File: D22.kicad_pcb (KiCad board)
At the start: 6 copper layers, 15 x 11 mm, 48 parts, among them IC1 AVR64DD28-I_STX, IC2 NCP730BM, IC3 DRV8231ADSGR, J1 Conn_02x08_Counter_Clockwise, J2 Conn_01x01, J3 Conn_01x01, J4 Conn_01x01, Q1 BC847BDW1, Q2 BC857BDW1, Q3 PMZB200UNEYL, Q4 PMZB200UNEYL, Q5 PMZB200UNEYL, Q6 PMZB200UNEYL

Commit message: mod: code cleanup
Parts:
- removed C4: 22u/25V, Capacitor_SMD:C_0603_1608Metric
- removed C7: 10u/25V, Capacitor_SMD:C_0603_1608Metric
- removed J3, J4: Conn_01x01, RTB:DummyNet-Connector
- added D4: SM5819L2-TP, RTB:SM5819L2TP, B.Cu at (62.5, -45.4)
- added IC4: NCP730BM, Package_SON:WSON-6-1EP_2x2mm_P0.65mm_EP1x1.6mm, B.Cu at (65.9, -46.0)
- added R23: 100, Resistor_SMD:R_0603_1608Metric, B.Cu at (62.1, -46.7)
- added R24: 10k, Resistor_SMD:R_0402_1005Metric, B.Cu at (59.5, -47.9)
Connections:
- net SUSI.dat renamed CAP_ENA
- IC1 pad 22: (no net) -> unconnected-(IC1-PF6_(~{RESET})-Pad22)
- IC2 pad 2: Net-(IC2-Pad2) -> unconnected-(IC2-NC/ADJ-Pad2)
- IC2 pad 4: (no net) -> unconnected-(IC2-EN-Pad4)
- IC2 pad 5: (no net) -> unconnected-(IC2-NC/PG-Pad5)
- J1 pad 14: VHBR -> CAP+
- J1 pad 7: (no net) -> unconnected-(J1-Pin_7-Pad7)
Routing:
- net CAP+: track 0.00 -> 5.32 mm, vias 0 -> 1
- net Net-(IC4-OUT): track 0.00 -> 4.81 mm
- net VHBR: track 22.0 -> 18.3 mm, vias 5 -> 2
- net CAP_ENA: track 19.5 -> 22.5 mm, vias 1 -> 2
- net +3V3: track 27.0 -> 26.1 mm
- net GND: track 32.9 -> 33.8 mm, vias 13 -> 12
- net AUX3: track 15.4 -> 14.8 mm
- net M1: track 23.4 -> 22.7 mm
- net SUSI.clk: vias 2 -> 1
- added copper zone on B.Cu, net unconnected-(IC2-NC/ADJ-Pad2)
- removed copper zone on B.Cu, net Net-(IC2-Pad2)
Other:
- board text added: "D22.1"
- board text removed: "D22.0"

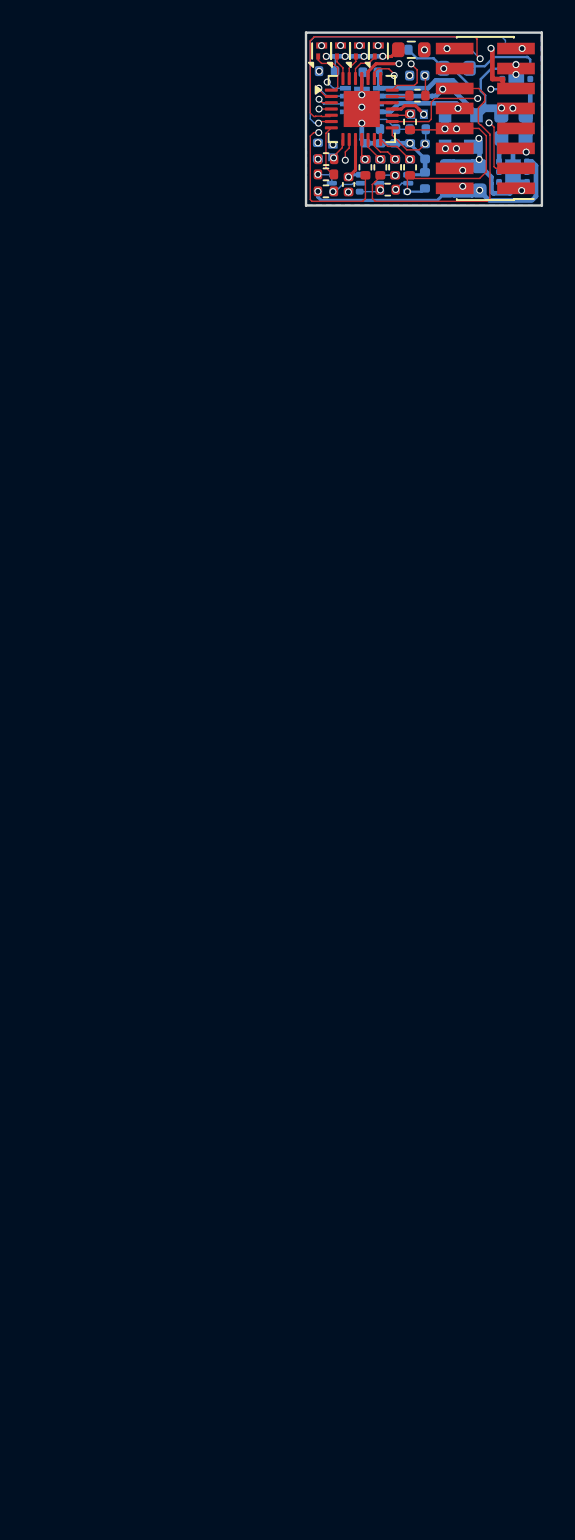
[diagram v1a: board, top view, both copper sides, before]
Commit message: add: 15V LDO for backup cap
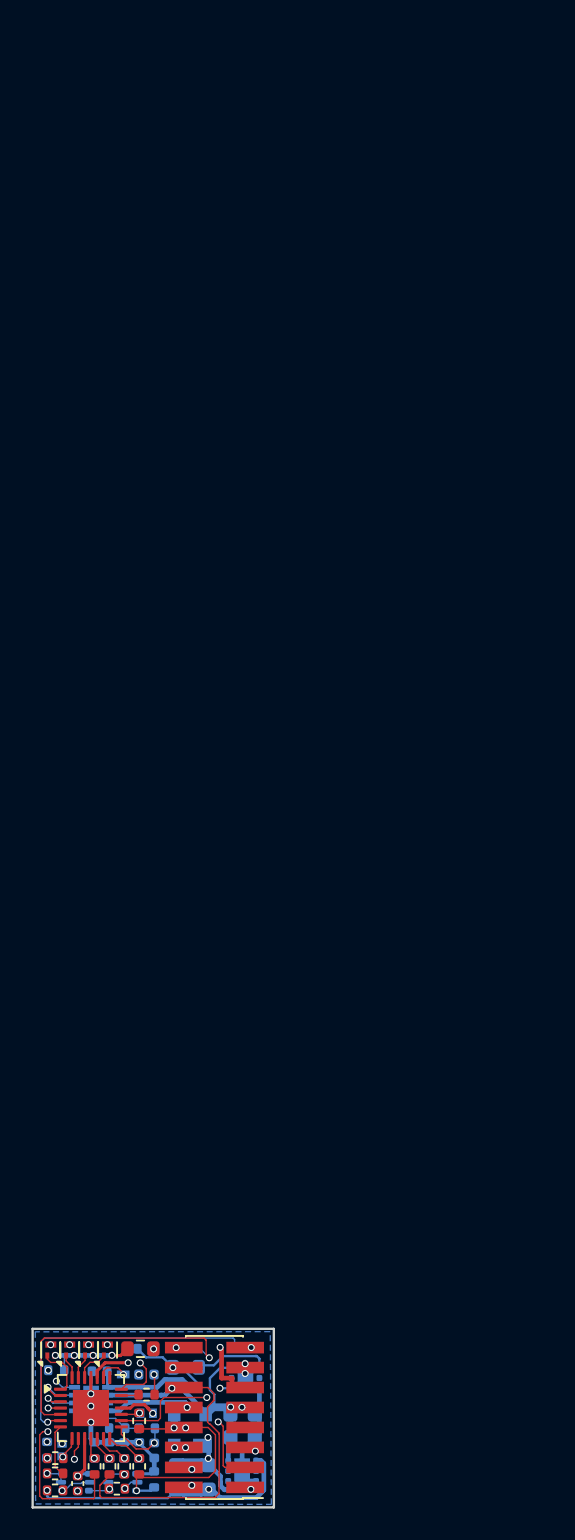
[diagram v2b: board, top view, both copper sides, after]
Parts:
- C1, C2: value 22u/25V -> 10u/25V
- C10, C8: value 100n -> 100n/50V
- C6: value 1u -> 1u/50V
- IC2: value NCP730BM -> NCP730BMT500TBG
- IC4: value NCP730BM -> NCP730BMT1500TBG
- J2: footprint RTB:DummyNet-Connector -> RTB:Solder 0.8 x 0.5
- moved C1 84.4 mm to (48.5, 40.4)
- moved C10 84.4 mm to (39.4, 36.2)
- moved C2 84.4 mm to (48.5, 39.0)
- moved C3 84.4 mm to (44.3, 43.0)
- moved C5 84.4 mm to (46.3, 43.0)
- moved C6 84.4 mm to (42.8, 41.3)
- moved C8 84.4 mm to (38.0, 43.4)
- moved D1 84.4 mm to (42.4, 38.9)
- moved D2 84.4 mm to (37.0, 41.2)
- moved D3 84.4 mm to (42.3, 36.4)
- moved D4 84.4 mm to (45.2, 37.3)
- moved D8 84.4 mm to (45.1, 40.3)
- moved IC1 84.4 mm to (38.8, 38.6)
- moved IC2 84.4 mm to (48.4, 42.6)
- moved IC3 84.4 mm to (38.8, 38.0)
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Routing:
- net CAP_ENA: track 22.5 -> 21.9 mm
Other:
- board size 15 x 11 mm -> 15.3 x 11.4 mm
